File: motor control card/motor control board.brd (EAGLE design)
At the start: 100 x 80 mm, 13 parts, among them J1 09231486921, J2 TBP02R1-381-07BE, J3 TBP02R1-381-07BE

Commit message: changed pinouts for the boards, next I have to make accomodations for new pinouts and the USB selector system
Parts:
- added SJ4, SJ5: SOLDERJUMPERTRACE, SparkFun-Passives:SJ_2S-TRACE
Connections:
- net EXT_1 renamed USB1_D-
- net EXT_2 renamed USB1_D+
- net EXT_3 renamed USB2_D-
- net EXT_4 renamed USB2_D+
- net EXT_5 renamed USB3_D-
- net EXT_6 renamed USB3_D+
- removed net EXT_7: J1.48
- new net N$11: SJ5.2, U$1.RESET
- new net N$5: SJ4.2, U$2.RESET
- new net RESET: J1.48, SJ4.1, SJ5.1, U$3.10@JP1
- net 3.3V: now also J1.23, J1.7; no longer J1.38
- net 5V: now also J1.38; no longer J1.23, J1.7
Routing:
- net 3.3V: track 214.9 -> 226.7 mm
- net 5V: track 5.08 -> 0.00 mm
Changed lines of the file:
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@@
 <grid distance="1" unitdist="mm" unit="mm" style="lines" multiple="1" display="no" altdistance="0.1" altunitdist="mm" altunit="mm"/>
 <layers>
-<layer number="1" name="Top" color="4" fill="1" visible="no" active="yes"/>
+<layer number="1" name="Top" color="4" fill="1" visible="yes" active="yes"/>
 <layer number="2" name="Route2" color="16" fill="1" visible="no" active="no"/>
 <layer number="3" name="Route3" color="17" fill="1" visible="no" active="no"/>
@@
 <layer number="14" name="Route14" color="22" fill="1" visible="no" active="no"/>
 <layer number="15" name="Route15" color="23" fill="1" visible="no" active="no"/>
-<layer number="16" name="Bottom" color="1" fill="1" visible="no" active="yes"/>
+<layer number="16" name="Bottom" color="1" fill="1" visible="yes" active="yes"/>
 <layer number="17" name="Pads" color="2" fill="1" visible="yes" active="yes"/>
 <layer number="18" name="Vias" color="2" fill="1" visible="yes" active="yes"/>
@@
 <class number="0" name="default" width="0" drill="0">
 </class>
+<class number="1" name="POWER" width="0" drill="0">
+<clearance class="1" value="0.508"/>
+</class>
 <class number="2" name="GND" width="0.3048" drill="0">
 <clearance class="0" value="0.3048"/>
@@
 <attribute name="PURCHASE-URL" value="https://pricing.snapeda.com/search/part/TBP02R1-381-07BE/?ref=eda" x="95" y="66.86" size="1.778" layer="27" rot="R270" display="off"/>
 </element>
+<element name="SJ4" library="SparkFun-Passives" package="SJ_2S-TRACE" value="SOLDERJUMPERTRACE" x="-11" y="3" smashed="yes">
+<attribute name="NAME" x="-11.9525" y="4.27" size="0.4064" layer="25"/>
+<attribute name="VALUE" x="-11.9525" y="1.349" size="0.4064" layer="27"/>
+</element>
+<element name="SJ5" library="SparkFun-Passives" package="SJ_2S-TRACE" value="SOLDERJUMPERTRACE" x="-14" y="3" smashed="yes">
+<attribute name="NAME" x="-14.9525" y="4.27" size="0.4064" layer="25"/>
+<attribute name="VALUE" x="-14.9525" y="1.349" size="0.4064" layer="27"/>
+</element>
 </elements>
 <signals>
@@
 <signal name="5V">
 <contactref element="J1" pad="39"/>
-<contactref element="J1" pad="23"/>
-<contactref element="J1" pad="7"/>
-<wire x1="10.68" y1="36.24" x2="5.6" y2="36.24" width="0.508" layer="16"/>
-<wire x1="10.68" y1="36.24" x2="8.14" y2="36.24" width="0" layer="19" extent="1-1"/>
+<contactref element="J1" pad="38"/>
+<wire x1="10.68" y1="33.7" x2="10.68" y2="36.24" width="0" layer="19" extent="1-1"/>
 </signal>
 <signal name="3.3V">
-<contactref element="J1" pad="38"/>
 <contactref element="U$1" pad="IOREF"/>
 <contactref element="U$1" pad="SLEEP"/>
@@
 <contactref element="J2" pad="2"/>
 <contactref element="J3" pad="2"/>
-<wire x1="10.68" y1="33.7" x2="14.3" y2="33.7" width="1.5" layer="1"/>
-<wire x1="14.3" y1="33.7" x2="18.5" y2="29.5" width="1.5" layer="1"/>
-<wire x1="18.5" y1="29.5" x2="18.5" y2="20.6" width="1.5" layer="1"/>
+<wire x1="18.5" y1="20.6" x2="18.5" y2="29.5" width="1.5" layer="1"/>
 <wire x1="95" y1="31.19" x2="89.19" y2="37" width="0.508" layer="1"/>
 <wire x1="52.25" y1="48.3" x2="54.5" y2="48.3" width="1.5" layer="1"/>
@@
 <wire x1="51.5124" y1="67.8824" x2="51.330025" y2="67.8824" width="1.5" layer="16"/>
 <wire x1="51.330025" y1="67.8824" x2="48.1952" y2="64.747575" width="1.5" layer="16"/>
+<contactref element="J1" pad="7"/>
+<contactref element="J1" pad="23"/>
+<wire x1="12.5" y1="35.5" x2="18.5" y2="29.5" width="1.5" layer="1"/>
+<wire x1="8.14" y1="36.24" x2="5.6" y2="36.24" width="1.5" layer="1"/>
+<wire x1="11.9" y1="36.1" x2="12.5" y2="35.5" width="0.6" layer="1"/>
+<wire x1="10.1464" y1="37.4464" x2="11.1797125" y2="37.4464" width="0.6" layer="1"/>
+<wire x1="10.1802875" y1="35.0336" x2="11.1797125" y2="35.0336" width="0.6" layer="1"/>
+<wire x1="11.47305625" y1="35.32694375" x2="11.1797125" y2="35.0336" width="0.6" layer="1"/>
+<wire x1="8.14" y1="36.24" x2="8.9738875" y2="36.24" width="1.5" layer="1"/>
+<wire x1="8.9738875" y1="36.24" x2="10.1802875" y2="35.0336" width="0.6" layer="1"/>
+<wire x1="12.5" y1="35.5" x2="12.32694375" y2="35.32694375" width="0.6" layer="1"/>
+<wire x1="12.32694375" y1="35.32694375" x2="11.47305625" y2="35.32694375" width="0.6" layer="1"/>
+<wire x1="10.1464" y1="37.4464" x2="8.9738875" y2="36.2738875" width="0.6" layer="1"/>
+<wire x1="8.9738875" y1="36.2738875" x2="8.9738875" y2="36.24" width="0.6" layer="1"/>
+<wire x1="11.9" y1="36.7261125" x2="11.9" y2="36.1" width="0.6" layer="1"/>
+<wire x1="11.1797125" y1="37.4464" x2="11.9" y2="36.7261125" width="0.6" layer="1"/>
 </signal>
 <signal name="SCK">
@@
 <wire x1="23.9304" y1="55.12396875" x2="23.9304" y2="51.61603125" width="0.508" layer="1"/>
 </signal>
-<signal name="EXT_1">
+<signal name="USB1_D-">
 <contactref element="J1" pad="15"/>
 </signal>
-<signal name="EXT_3">
+<signal name="USB2_D-">
 <contactref element="J1" pad="31"/>
 </signal>
-<signal name="EXT_5">
+<signal name="USB3_D-">
 <contactref element="J1" pad="46"/>
 </signal>
-<signal name="EXT_7">
+<signal name="RESET">
 <contactref element="J1" pad="48"/>
-</signal>
-<signal name="EXT_6">
+<contactref element="U$3" pad="10@JP1"/>
+<contactref element="SJ5" pad="1"/>
+<contactref element="SJ4" pad="1"/>
+<wire x1="10.68" y1="59.1" x2="30.27" y2="66.13" width="0" layer="19" extent="1-1"/>
+<wire x1="-11.508" y1="3" x2="10.68" y2="59.1" width="0" layer="19" extent="1-1"/>
+<wire x1="-14.508" y1="3" x2="-11.508" y2="3" width="0" layer="19" extent="1-1"/>
+</signal>
+<signal name="USB3_D+">
 <contactref element="J1" pad="47"/>
 </signal>
-<signal name="EXT_4">
+<signal name="USB2_D+">
 <contactref element="J1" pad="32"/>
 </signal>
-<signal name="EXT_2">
+<signal name="USB1_D+">
 <contactref element="J1" pad="16"/>
 </signal>
@@
 <contactref element="U$3" pad="3@JP2"/>
 </signal>
+<signal name="N$5">
+<contactref element="U$2" pad="RESET"/>
+<contactref element="SJ4" pad="2"/>
+<wire x1="-10.492" y1="3" x2="52.25" y2="37.16" width="0" layer="19" extent="1-1"/>
+</signal>
+<signal name="N$11">
+<contactref element="U$1" pad="RESET"/>
+<contactref element="SJ5" pad="2"/>
+<wire x1="-13.492" y1="3" x2="52.25" y2="71.16" width="0" layer="19" extent="1-1"/>
+</signal>
 </signals>

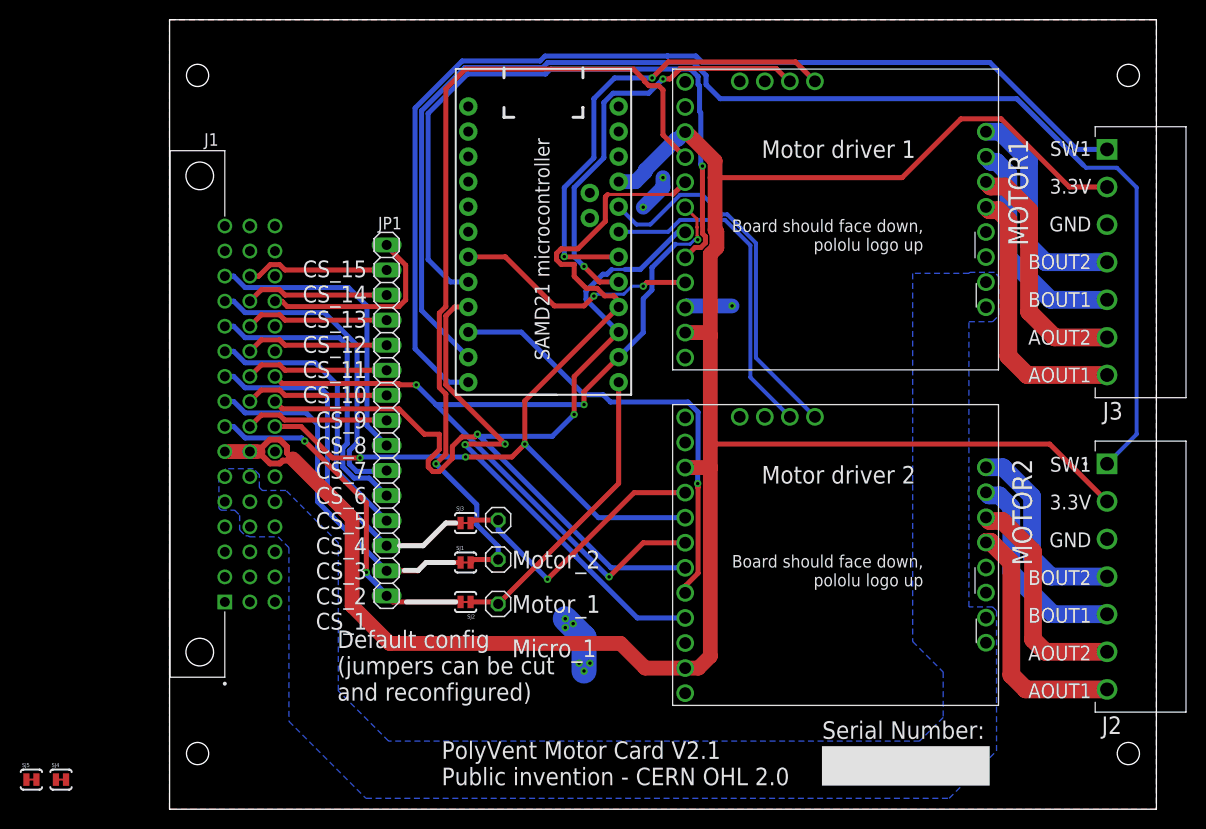
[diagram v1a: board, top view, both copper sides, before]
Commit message: made card holes bigger, started usb port work, but I'm not done that part yet
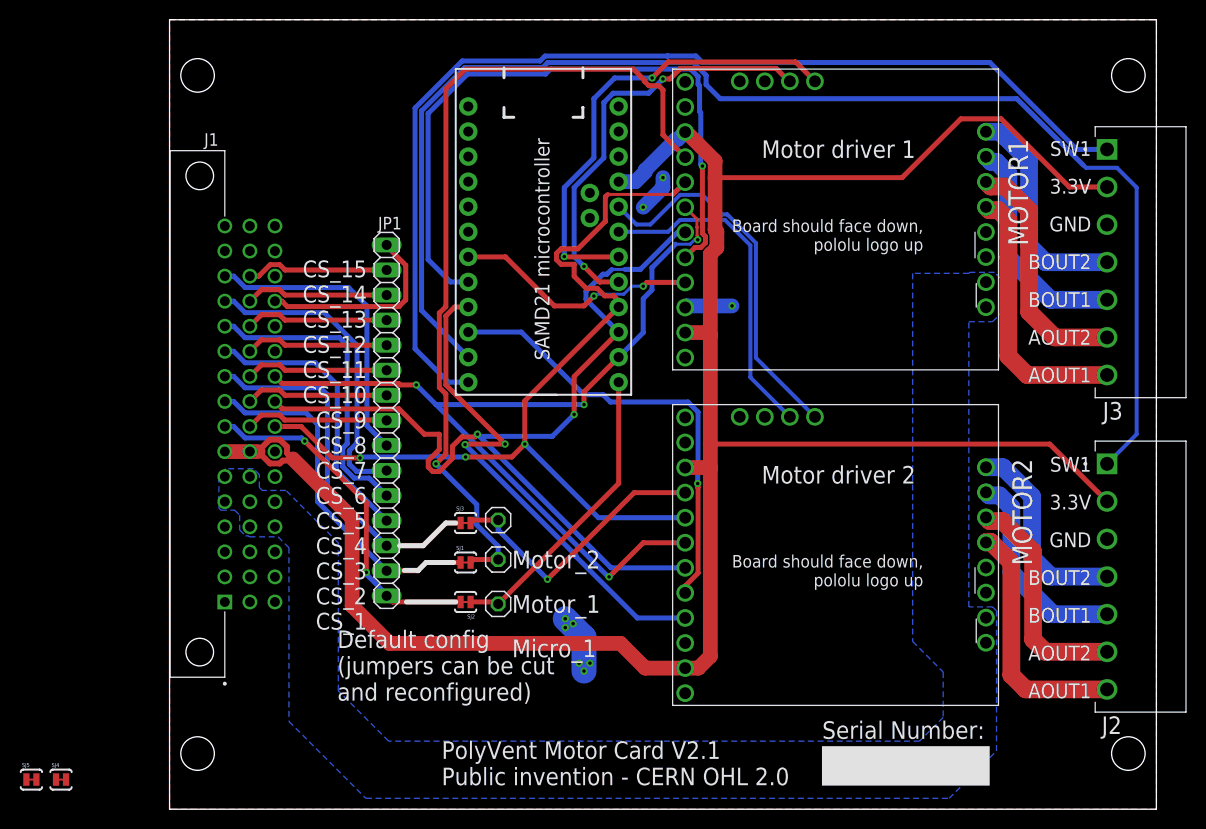
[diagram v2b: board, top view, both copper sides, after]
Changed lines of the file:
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@@
 <wire x1="100" y1="80" x2="0" y2="80" width="0" layer="20"/>
 <wire x1="0" y1="80" x2="0" y2="0" width="0" layer="20"/>
-<hole x="2.84" y="5.64" drill="2.25"/>
-<hole x="2.84" y="74.36" drill="2.25"/>
-<hole x="97.16" y="74.36" drill="2.25"/>
-<hole x="97.16" y="5.64" drill="2.25"/>
+<hole x="2.84" y="5.64" drill="3.4"/>
+<hole x="2.84" y="74.36" drill="3.4"/>
+<hole x="97.16" y="74.36" drill="3.4"/>
+<hole x="97.16" y="5.64" drill="3.4"/>
 <text x="20" y="18.2" size="1.7" layer="25" align="bottom-right">CS_15
 CS_14

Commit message: USB system mods complete on the main board, valves board, and motor board
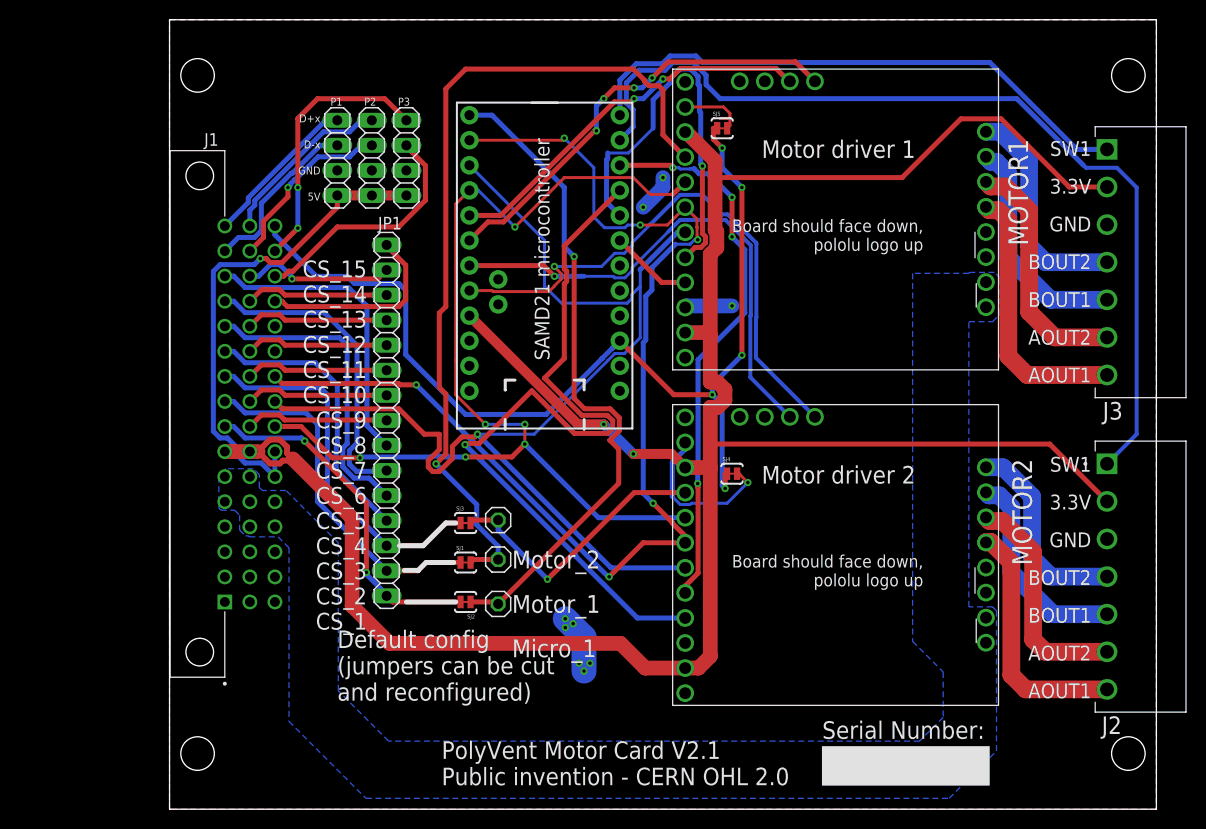
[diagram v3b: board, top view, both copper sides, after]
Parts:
- removed U$3: (no value), SparkFun-SAMD21-Mini-Breakout:JP1_SPARKFUN-SAMD21-MINI-BREAKOUT-V10
- added JP5, JP6, JP7: (no value), pinhead:1X04
- added U$4: (no value), SparkFun-SAMD21-Mini-Breakout:JP1_SPARKFUN-SAMD21-MINI-BREAKOUT-V10
- moved SJ5 96.2 mm to (56.0, 69.0)
- moved SJ4 74.7 mm to (57.0, 34.0)
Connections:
- new net N$13: U$4.2@JP2
- net 3.3V: now also U$4.4@JP2; no longer U$3.4@JP2
- net 5V: now also JP5.1, JP6.1, JP7.1
- net AREF: now also U$4.3@JP2; no longer U$3.3@JP2
- net BEMF1: now also U$4.7@JP2; no longer U$3.7@JP2
- net BEMF2: now also U$4.5@JP2; no longer U$3.5@JP2
- net DIR1: now also U$4.5@JP1; no longer U$3.5@JP1
- net DIR2: now also U$4.3@JP1; no longer U$3.3@JP1
- net GND: now also JP5.2, JP6.2, JP7.2, U$4.9@JP1; no longer U$3.2@JP2, U$3.9@JP1
- net MISO: now also U$4.10@JP2; no longer U$3.10@JP2
- net MOSI: now also U$4.11@JP2; no longer U$3.11@JP2
- net RESET: now also U$4.10@JP1; no longer U$3.10@JP1
- net SCK: now also U$4.9@JP2; no longer U$3.9@JP2
- net SS: now also U$4.12@JP2; no longer U$3.12@JP2
- net STALL1: now also U$4.8@JP2; no longer U$3.8@JP2
- net STALL2: now also U$4.6@JP2; no longer U$3.6@JP2
- net STEP1: now also U$4.6@JP1; no longer U$3.6@JP1
- net STEP2: now also U$4.4@JP1; no longer U$3.4@JP1
- net SW1: now also U$4.2@JP1; no longer U$3.2@JP1
- net SW2: now also U$4.1@JP1; no longer U$3.1@JP1
- net USB1_D+: now also JP5.4
- net USB1_D-: now also JP5.3
- net USB2_D+: now also JP6.4
- net USB2_D-: now also JP6.3
- net USB3_D+: now also JP7.4
- net USB3_D-: now also JP7.3
- net VIN: now also U$4.1@JP2; no longer U$3.1@JP2
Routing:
- net RESET: track 0.00 -> 103.5 mm, vias 0 -> 5
- net 5V: track 0.00 -> 51.1 mm, vias 0 -> 1
- net SW2: track 107.4 -> 57.9 mm
- net SW1: track 136.4 -> 94.3 mm
- net SS: track 30.4 -> 67.4 mm, vias 0 -> 1
- net STEP2: track 51.8 -> 80.8 mm, vias 2 -> 1
- net MOSI: track 93.0 -> 120.5 mm, vias 4 -> 6
- net DIR1: track 69.2 -> 41.7 mm
- net USB3_D+: track 0.00 -> 27.1 mm, vias 0 -> 2
- net USB3_D-: track 0.00 -> 24.8 mm
- net MISO: track 95.0 -> 116.6 mm, vias 2 -> 1
- net 3.3V: track 226.7 -> 248.1 mm, vias 0 -> 2
- net STALL2: track 34.0 -> 53.8 mm, vias 0 -> 1
- net BEMF2: track 38.0 -> 57.2 mm, vias 0 -> 1
- net USB2_D-: track 0.00 -> 18.4 mm, vias 0 -> 1
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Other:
- board text added: "D+x D-x GND 5V"
- board text added: "P1 P2 P3"

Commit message: did some small correction work on the boards
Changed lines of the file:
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@@
 <grid distance="1" unitdist="mm" unit="mm" style="lines" multiple="1" display="no" altdistance="0.1" altunitdist="mm" altunit="mm"/>
 <layers>
-<layer number="1" name="Top" color="4" fill="1" visible="yes" active="yes"/>
+<layer number="1" name="Top" color="4" fill="1" visible="no" active="yes"/>
 <layer number="2" name="Route2" color="16" fill="1" visible="no" active="no"/>
 <layer number="3" name="Route3" color="17" fill="1" visible="no" active="no"/>
@@
 <layer number="14" name="Route14" color="22" fill="1" visible="no" active="no"/>
 <layer number="15" name="Route15" color="23" fill="1" visible="no" active="no"/>
-<layer number="16" name="Bottom" color="1" fill="1" visible="yes" active="yes"/>
+<layer number="16" name="Bottom" color="1" fill="1" visible="no" active="yes"/>
 <layer number="17" name="Pads" color="2" fill="1" visible="yes" active="yes"/>
 <layer number="18" name="Vias" color="2" fill="1" visible="yes" active="yes"/>
@@
 <rectangle x1="72.61" y1="-4.11" x2="76.61" y2="12.89" layer="25" rot="R90"/>
 <text x="82.6" y="8.91" size="1.778" layer="25" rot="R180">Serial Number:</text>
-<text x="27.57" y="2.43" size="1.778" layer="25">PolyVent Motor Card V2.1
+<text x="29.97" y="5.23" size="1.778" layer="25">PolyVent Motor Card V2.1
 Public invention - CERN OHL 2.0</text>
 <text x="15.3" y="70.4" size="0.8" layer="25" distance="230" align="top-right">D+x
